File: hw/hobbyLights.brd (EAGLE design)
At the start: 50 x 35 mm, 56 parts, among them U1 MCP73831-2, U2 POWER, U3 BD48K28G, U4 ATMEGA32U4-AU, U5 TPS61222, Y1 RESONATORSMD

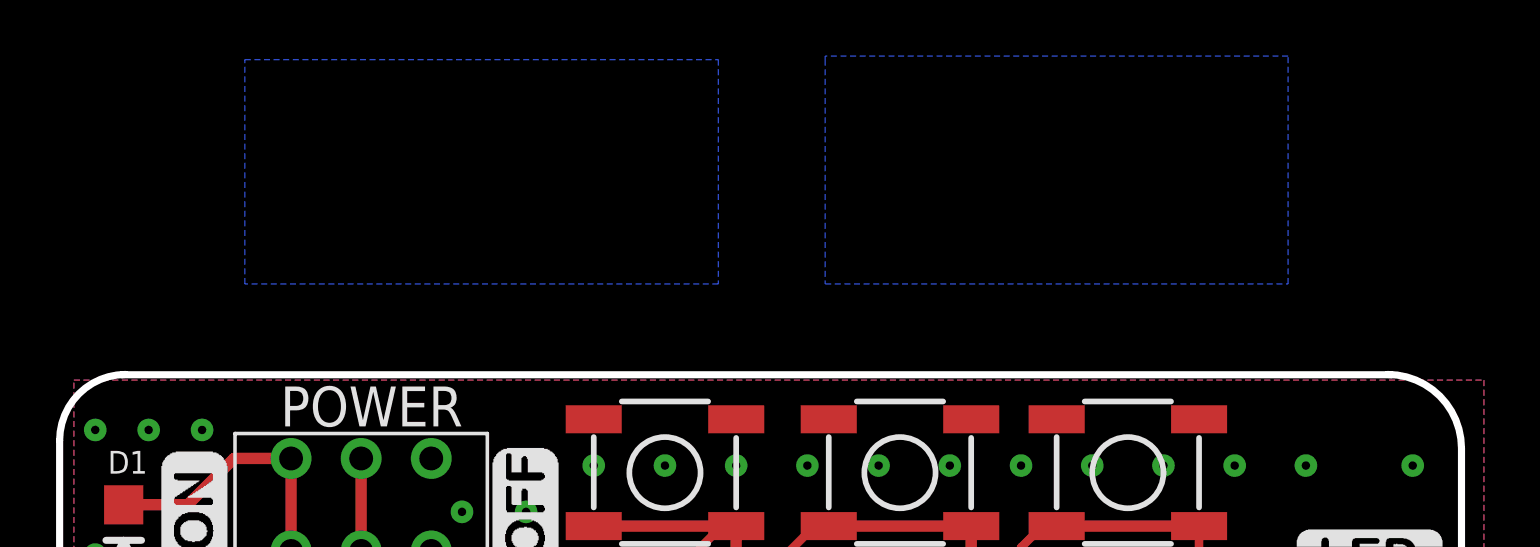
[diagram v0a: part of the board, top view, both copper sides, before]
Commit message: Added daughter boards for high side switching.
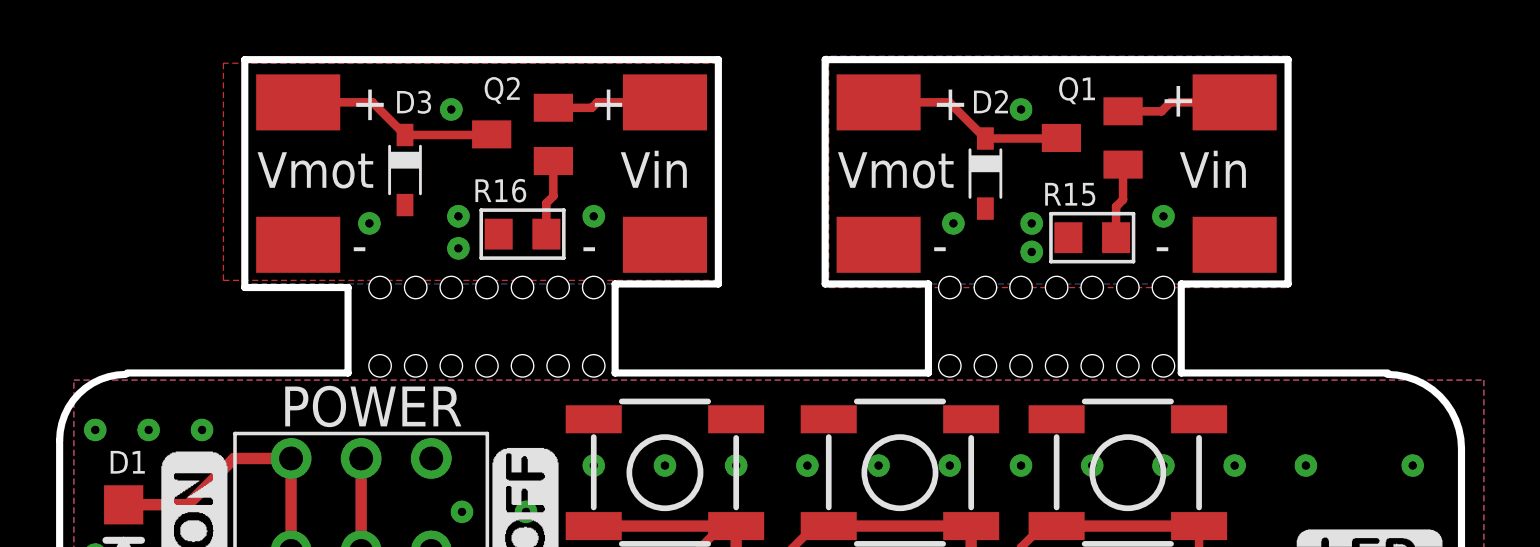
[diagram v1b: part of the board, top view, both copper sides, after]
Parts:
- added D2, D3: BAT60J, diode:SOD323_ST
- added MOT, MOT1, U$12, U$13, U$14, U$15, VIN, VIN1: TP_3X2, fmc:TP
- added Q1, Q2: BC857BSMD, transistor-pnp:SOT23-BEC
- added R15, R16: 1K, rcl:R0603
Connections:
- new net DGND: D2.A, D3.A, R15.1, R16.1, U$12.P$1, U$13.P$1, U$14.P$1, U$15.P$1
- new net N$1: Q1.B, R15.2
- new net N$11: Q1.E, VIN.P$1
- new net N$24: Q2.B, R16.2
- new net N$25: D3.C, MOT1.P$1, Q2.C
- new net N$26: Q2.E, VIN1.P$1
- new net N$8: D2.C, MOT.P$1, Q1.C
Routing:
- net N$25: track 0.00 -> 7.39 mm
- net N$8: track 0.00 -> 7.06 mm
- net N$11: track 0.00 -> 4.11 mm
- net N$26: track 0.00 -> 4.06 mm
- net N$1: track 0.00 -> 2.71 mm
- net N$24: track 0.00 -> 2.71 mm
- added copper zone on layer 1, net DGND
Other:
- board size 50 x 35 mm -> 50 x 46.2 mm
- board text added: "Vin"
- board text added: "Vmot"

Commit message: Updated diodes and added frames.
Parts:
- D2, D3: value BAT60J -> NSR0240HT1G
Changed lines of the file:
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@@
 <attribute name="VALUE" x="34.925" y="37.973" size="0.8128" layer="27" ratio="12"/>
 </element>
-<element name="D2" library="diode" package="SOD323_ST" value="BAT60J" x="33.02" y="42.164" smashed="yes" rot="R270">
+<element name="D2" library="diode" package="SOD323_ST" value="NSR0240HT1G" x="33.02" y="42.164" smashed="yes" rot="R270">
 <attribute name="NAME" x="32.513" y="44.311" size="0.8128" layer="25" ratio="12"/>
 <attribute name="VALUE" x="31.02" y="43.814" size="1.27" layer="27" rot="R270"/>
@@
 </element>
 <element name="R16" library="rcl" package="R0603" value="1K" x="16.51" y="40.005"/>
-<element name="D3" library="diode" package="SOD323_ST" value="BAT60J" x="12.319" y="42.291" smashed="yes" rot="R270">
+<element name="D3" library="diode" package="SOD323_ST" value="NSR0240HT1G" x="12.319" y="42.291" smashed="yes" rot="R270">
 <attribute name="NAME" x="11.939" y="44.311" size="0.8" layer="25" ratio="12"/>
 <attribute name="VALUE" x="10.319" y="43.941" size="1.27" layer="27" rot="R270"/>

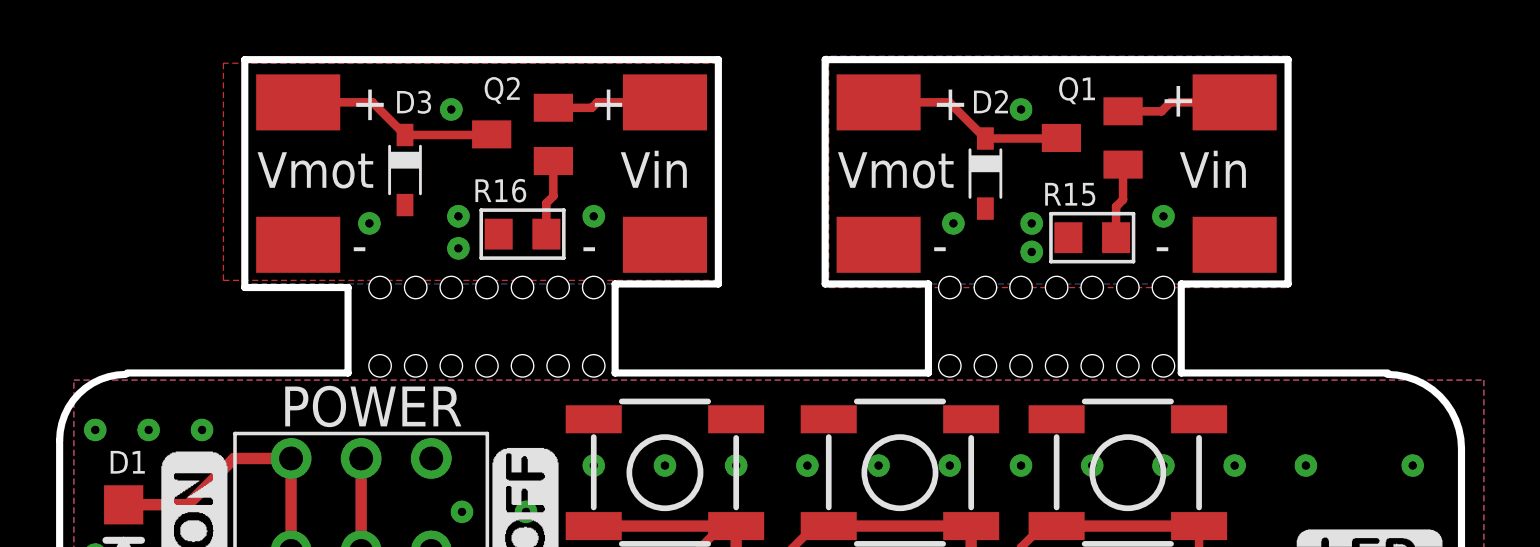
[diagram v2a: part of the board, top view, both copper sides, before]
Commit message: Removed side boards.
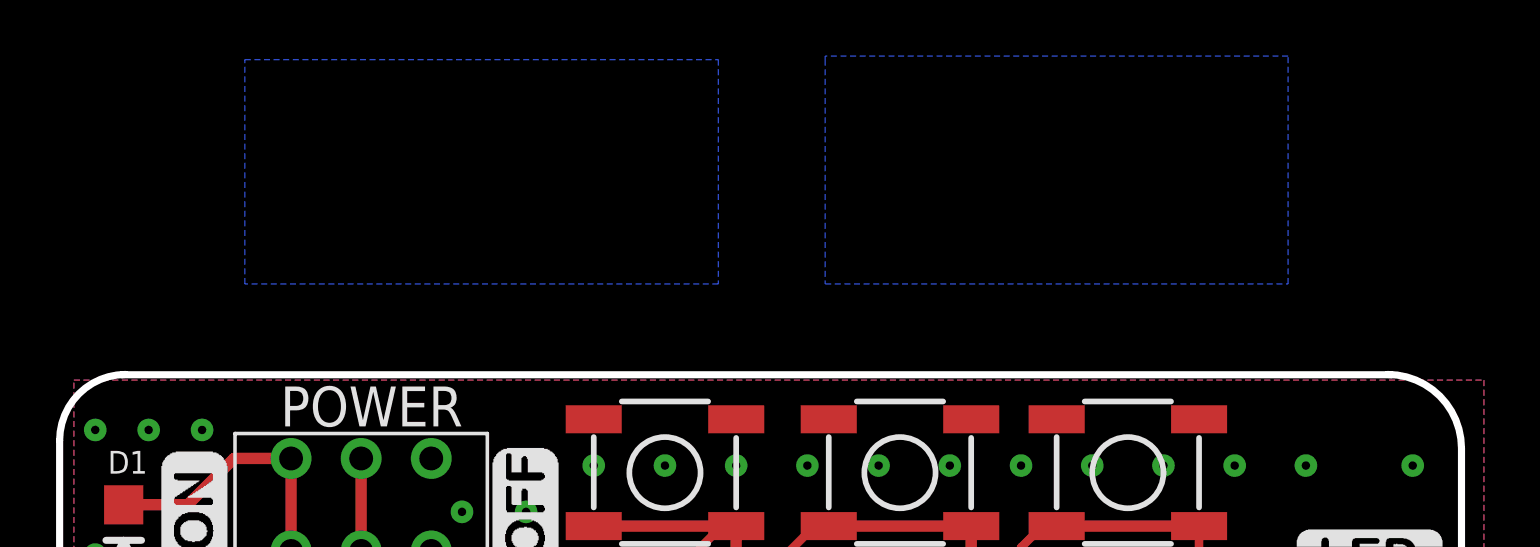
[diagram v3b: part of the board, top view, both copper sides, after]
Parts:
- removed D2, D3: NSR0240HT1G, diode:SOD323_ST
- removed MOT, MOT1, U$12, U$13, U$14, U$15, VIN, VIN1: TP_3X2, fmc:TP
- removed Q1, Q2: BC857BSMD, transistor-pnp:SOT23-BEC
- removed R15, R16: 1K, rcl:R0603
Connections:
- removed net DGND: D2.A, D3.A, R15.1, R16.1, U$12.P$1, U$13.P$1, U$14.P$1, U$15.P$1
- removed net N$1: Q1.B, R15.2
- removed net N$11: Q1.E, VIN.P$1
- removed net N$24: Q2.B, R16.2
- removed net N$25: D3.C, MOT1.P$1, Q2.C
- removed net N$26: Q2.E, VIN1.P$1
- removed net N$8: D2.C, MOT.P$1, Q1.C
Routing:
- net N$25: track 7.39 -> 0.00 mm
- net N$8: track 7.06 -> 0.00 mm
- net N$11: track 4.11 -> 0.00 mm
- net N$26: track 4.06 -> 0.00 mm
- net N$1: track 2.71 -> 0.00 mm
- net N$24: track 2.71 -> 0.00 mm
- removed copper zone on layer 1, net DGND
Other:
- board size 50 x 46.2 mm -> 50 x 35 mm
- board text removed: "Vin"
- board text removed: "Vmot"
